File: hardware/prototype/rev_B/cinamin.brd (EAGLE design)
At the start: 89 x 44.5 mm, 45 parts, among them U1 AP4400_3.4_2.3, U6 AP4400_3.4_2.3, X1 16Mhz, X3 16Mhz

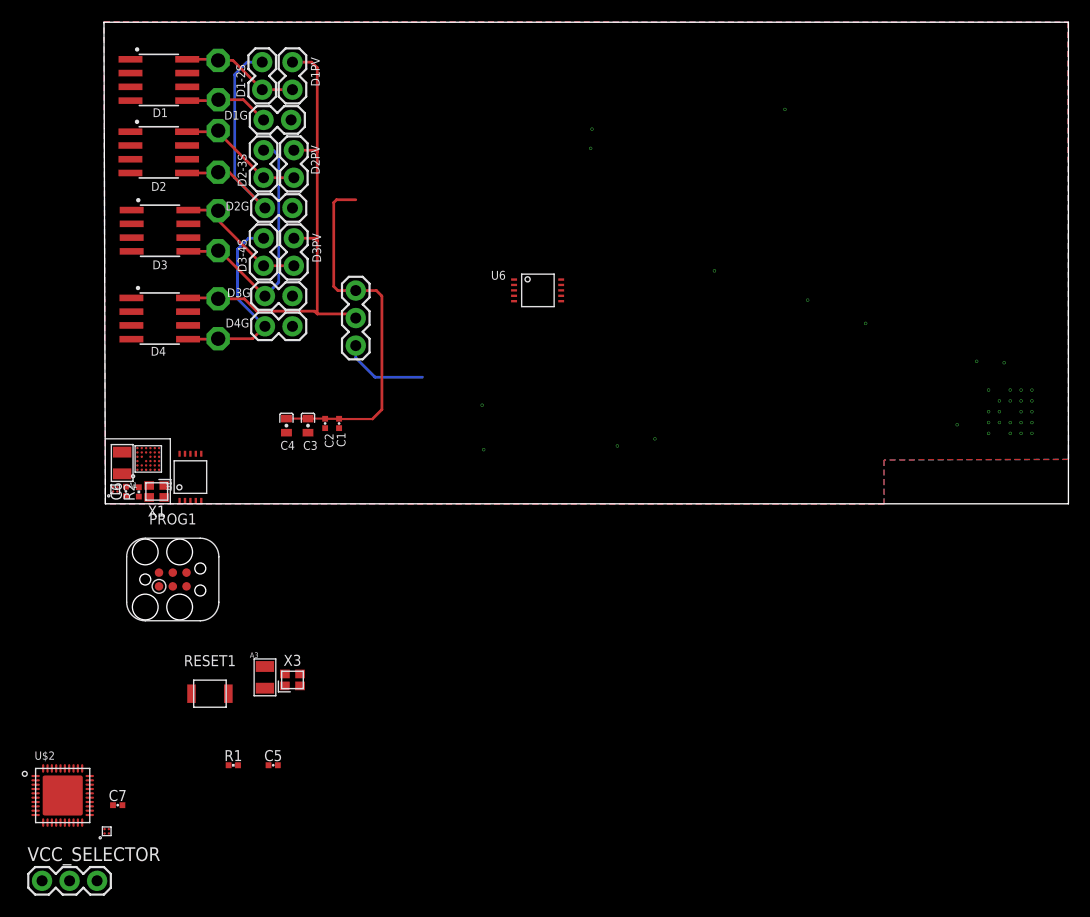
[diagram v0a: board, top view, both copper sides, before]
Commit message: prototype board mostly done, clean up board and schematic before ordering tonight
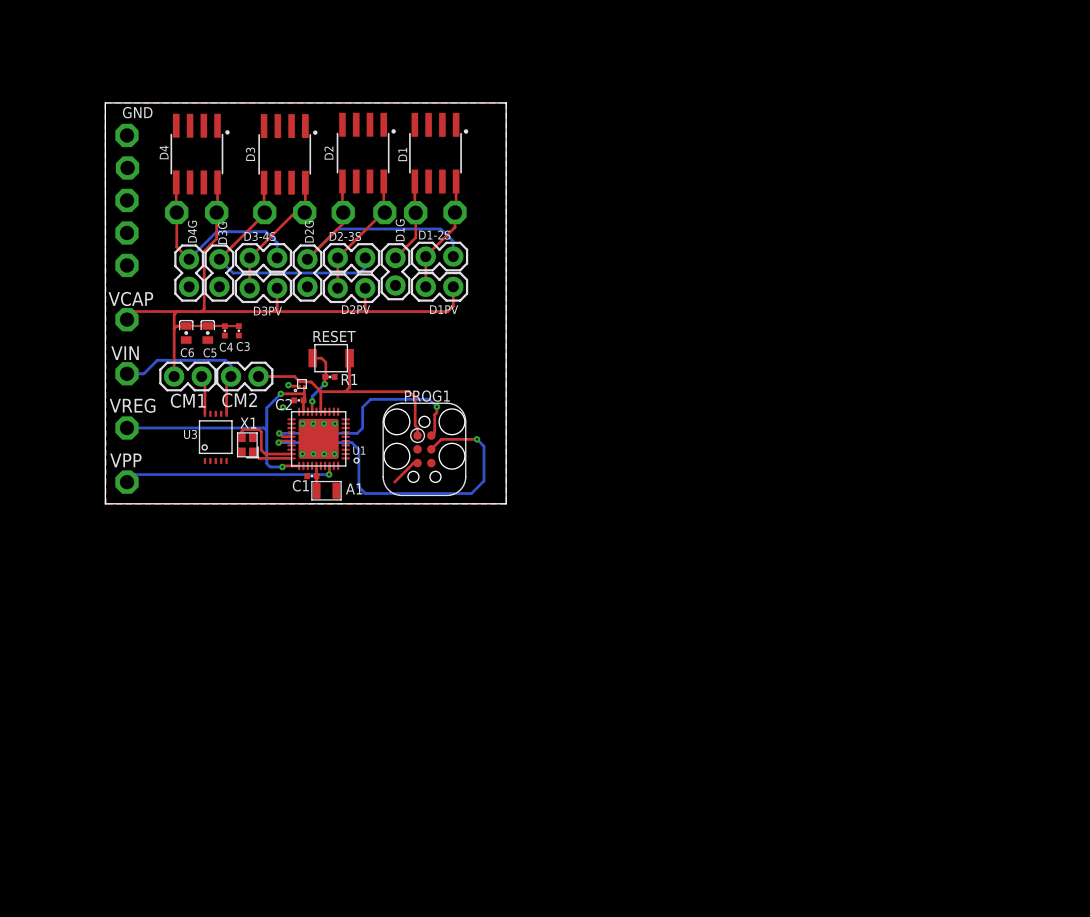
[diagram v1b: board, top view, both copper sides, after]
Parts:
- removed A3: AH212M, chips:AH212M
- removed C7: 1pF, passives:0402_CAP
- removed PV_TO_CAP, VCC_SELECTOR: (no value), SparkFun-Connectors:1X03
- removed R2: 2.2k, passives:0402_RES
- removed RESET1: B3U-1000P, switches:B3U-1000P
- removed U$1, U$4: (no value), chips:FLIP_CHIP-4
- removed U$2: DA14581-40, chips:QFN-40-5MM
- removed U$3: DA14581-BGA, chips:WLCSP-34
- removed U6: AP4400_3.4_2.3, chips:TSOP-10
- removed X3: 16Mhz, crystals:TXC-8Y
- added CM1, CM2: (no value), SparkFun-Passives:1X02
- added RESET: B3U-1000P, switches:B3U-1000P
- added TP10, TP11, TP13, TP14, TP9, VCAP, VIN, VPP, VREG: TPSPAD1-13, testpad:P1-13
- added U2: (no value), chips:FLIP_CHIP-4
- added U3: AP4400_3.4_2.3, chips:TSOP-10
- C1: value 15uF -> 1pF
- C2: value 15uF -> 1uF
- C3, C4: value 100uF -> 15uF; device passives:CAP0603 -> passives:0402_CAP
- C5, C6: value 1uF -> 100uF; device passives:0402_CAP -> passives:CAP0603
- U1: value AP4400_3.4_2.3 -> DA14581-40; device chips:TSOP-10 -> chips:QFN-40-5MM
- moved C5 40.4 mm to (9.46, 15.8), turned to 270 degrees
- moved R1 36.9 mm to (20.7, 11.7), turned to 180 degrees
- moved D1 26.4 mm to (30.5, 32.4), turned to 180 degrees
- moved PROG1 26.2 mm to (29.5, 5.03), turned to 270 degrees
- moved TP3 26.0 mm to (32.3, 26.9), turned to 0 degrees
- moved D1PV 25.5 mm to (32.1, 20.0), turned to 180 degrees
- moved D1-2S 21.6 mm to (29.6, 22.8), turned to 0 degrees
- moved TP6 21.0 mm to (28.6, 26.9), turned to 0 degrees
- moved D2 18.9 mm to (23.8, 32.4), turned to 180 degrees
- moved D1G 18.1 mm to (26.8, 20.2), turned to 90 degrees
- moved A1 18.0 mm to (19.2, 1.21), turned to 270 degrees
- moved TP4 17.1 mm to (25.8, 26.9), turned to 0 degrees
- moved C6 15.6 mm to (7.46, 15.8), turned to 270 degrees
- moved D4 15.6 mm to (8.45, 32.3), turned to 180 degrees
- moved D2PV 14.3 mm to (24.0, 19.9), turned to 180 degrees
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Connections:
- removed net DA_VCC: RESET1.2, U$1.A2, U$1.B2, U$2.14, U$2.15, VCC_SELECTOR.2
- removed net N$10: C6.1, U$3.A2, U$3.F2, U$4.B1
- removed net N$5: U$3.B1, X1.3
- removed net N$6: U$3.E4, U$3.F4, U$4.A2, U$4.B2, U1.6
- removed net N$66: D1PV.1, D2PV.1, D3PV.1, D4.8, PV_TO_CAP.2, TP5.TP
- removed net N$8: A1.P1, U$3.A4
- removed net PV: PV_TO_CAP.1
- net GND: now also C3.2, C4.2, C5.NEG, C6.NEG, TP10.TP, TP11.TP, TP13.TP, TP14.TP, TP9.TP, U1.16, U1.23, U1.34, U1.PAD, U2.A1, U3.5; no longer C3.NEG, C4.NEG, C5.2, C6.2, C7.2, R2.1, U$1.A1, U$2.16, U$2.23, U$2.34, U$2.PAD, U$3.A3, U$3.E1, U$4.A1, U1.5, U6.5, X3.2, X3.4
- net N$1: now also C3.1, C4.1, C5.POS, C6.POS, CM1.1, D1PV.1, D2PV.1, D3PV.1, D4.8, TP5.TP, VCAP.TP; no longer C1.1, C2.1, C3.POS, C4.POS, PV_TO_CAP.3, U6.10
- net N$15: now also U1.29, X1.3; no longer U$2.29, X3.3
- net N$18: now also U1.30, X1.1; no longer U$2.30, X3.1
- net N$19: now also A1.P1, C1.1, U1.35; no longer A3.P1, C7.1, U$2.35
- net N$2: now also U1.38, VPP.TP; no longer R2.2, U$3.E3
- net N$22: now also RESET.1, U1.17; no longer RESET1.1, U$2.17
- net N$3: now also C2.1, U1.19, U1.31, U2.B1, VREG.TP; no longer C5.1, U$1.B1, U$2.19, U$2.31
- net N$4: now also CM2.1, U3.6, VIN.TP; no longer U6.6, VCC_SELECTOR.1
- net N$7: now also CM1.2, U3.10; no longer U$3.A1, X1.1
- net SWDIO: now also U1.25; no longer U$2.25, U$3.D1
- net SW_CLK: now also U1.26; no longer U$2.26, U$3.C1
- net VCC_EXT: now also CM2.2, RESET.2, U1.14, U1.15, U2.A2, U2.B2; no longer VCC_SELECTOR.3
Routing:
- net N$66: track 46.1 -> 0.00 mm
- net SW_CLK: track 0.00 -> 33.4 mm, vias 0 -> 2
- net N$3: track 0.00 -> 27.8 mm, vias 0 -> 2
- net N$1: track 34.5 -> 61.8 mm
- net VCC_EXT: track 0.00 -> 24.4 mm
- net SWDIO: track 0.00 -> 21.4 mm, vias 0 -> 2
- net N$2: track 0.00 -> 19.7 mm, vias 0 -> 1
- net N$4: track 0.00 -> 14.9 mm
- net PV: track 8.03 -> 0.00 mm
- net N$15: track 0.00 -> 7.46 mm
- net N$22: track 0.00 -> 6.45 mm, vias 0 -> 2
- net N$18: track 0.00 -> 3.97 mm
- net GND: track 0.00 -> 3.93 mm, vias 34 -> 10
- net N$7: track 0.00 -> 3.57 mm
- net N$19: track 0.00 -> 2.30 mm
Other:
- board size 89 x 44.5 mm -> 37 x 37 mm
- board text added: "Cinamin Beacon Evaluation Board Rev_B Joshua Adkins 05/2016"
- board text added: "GND"
- board text removed: "BQ"
- board text removed: "BQ25504"
- board text removed: "Bluetooth"
- board text removed: "Buffer Caps"
- board text removed: "CAP"
- board text removed: "Cinamin Beacon Evaluation Board Rev_A Joshua Adkins 08/2015"

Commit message: prototype to production
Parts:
- JP1: value HIGH -> PAR1
- JP10: value GND -> GND4
- JP11: value (none) -> CURRENT_MEASURE1
- JP12: value (none) -> CURRENT_MEASURE2
- JP2: value SER -> SER1
- JP3: value GND -> GND1
- JP4: value HIGH -> PAR2
- JP5: value SER -> SER2
- JP6: value GND -> GND2
- JP7: value HIGH -> PAR3
- JP8: value SER -> SER3
- JP9: value GND -> GND3
- TP1: value TPSPAD1-13 -> D3H
- TP10, TP11, TP13, TP14, TP9: value TPSPAD1-13 -> GND
- TP12: value TPSPAD1-13 -> VCAP
- TP15: value TPSPAD1-13 -> VDET
- TP16: value TPSPAD1-13 -> VREG
- TP17: value TPSPAD1-13 -> VPP
- TP2: value TPSPAD1-13 -> D2L
- TP3: value TPSPAD1-13 -> D1H
- TP4: value TPSPAD1-13 -> D2H
- TP5: value TPSPAD1-13 -> D4H
- TP6: value TPSPAD1-13 -> D1L
- TP7: value TPSPAD1-13 -> D3L
- TP8: value TPSPAD1-13 -> D4L
- U2: value (none) -> LD391151.4V
- moved A1 0.05 mm to (19.2, 1.26)
- renumbered CM1 to JP11, CM2 to JP12, D1-2S to JP2, D1G to JP3, D1PV to JP1, D2-3S to JP5, D2G to JP6, D2PV to JP4, D3-4S to JP8, D3G to JP9, D3PV to JP7, D4G to JP10, VCAP to TP12, VIN to TP15, VPP to TP17, VREG to TP16
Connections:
- net N$4 renamed DET_OUT
- net N$43 renamed JP10
- net N$7 renamed VCAP
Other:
- board text added: "PAR"
- board text added: "SER"
- board text added: "U2"
- board text added: "VCAP"
- board text added: "VDET"
- board text added: "VPP"
- board text added: "VREG"
